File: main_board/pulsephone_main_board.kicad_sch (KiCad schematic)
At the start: 44 parts, among them J1 USB_C_Receptacle_USB2.0_14P, J2 Conn_01x05, J3 Conn_2Rows-35Pins_MountingPin, J4 Conn_2Rows-35Pins_MountingPin, J5 Conn_2Rows-35Pins_MountingPin, U1 XL1509-3.3, U2 PCM5102APWR, U5 TP4056-42-ESOP8

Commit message: add sd card slot. also add rst and onoff buttons
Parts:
- added J7: Micro_SD_Card_Det1, Connector_Card:microSD_HC_Hirose_DM3AT-SF-PEJM5, symbol Connector:Micro_SD_Card_Det1
- added R5, R6: 10 kΩ, Resistor_SMD:R_0805_2012Metric, symbol Device:R
- added SW1, SW2: SW_Push, Button_Switch_SMD:SW_Tactile_SPST_NO_Straight_CK_PTS636Sx25SMTRLFS, symbol Switch:SW_Push
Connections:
- net +3.3V: now also R5.2, R6.2
- net GND: now also J7.6 (VSS), SW1.1, SW2.1
- net SD2_DAT0: now reaches MCM93_MOD1.72 (2)
- net SD2_DAT0: now also J7.7 (DAT0)
- net SD2_DAT1: now reaches MCM93_MOD1.73 (3)
- net SD2_DAT1: now also J7.8 (DAT1)
- net SD2_CD_B: now reaches MCM93_MOD1.74 (4)
- net SD2_CD_B: now also MCM93_MOD1.76 (6), J7.9 (DET)
- net SD2_VDD: now reaches MCM93_MOD1.134 (29)
- net SD2_VDD: now also J7.4 (VDD)
- net RESET: now reaches MCM93_MOD1.14
- net RESET: now also R5.1, SW1.2
- net ONOFF: now reaches MCM93_MOD1.3
- net ONOFF: now also R6.1, SW2.2
- net SD2_RST_B: now reaches MCM93_MOD1.65 (30)
- net SD2_DAT3: now reaches MCM93_MOD1.67 (32)
- net SD2_DAT3: now also J7.2 (DAT3/CD)
- net SD2_DAT2: now reaches MCM93_MOD1.68 (33)
- net SD2_DAT2: now also J7.1 (DAT2)
- net SD2_CMD: now reaches MCM93_MOD1.69 (34)
- net SD2_CMD: now also J7.3 (CMD)
- net SD2_CLK: now reaches MCM93_MOD1.70 (35)
- net SD2_CLK: now also J7.5 (CLK)
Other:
- note added: "Active Low ONOFF"
- note added: "Active Low Reset"
- note added: "MICRO SD"
- moved on the sheet: BT1, C1, C10, C11, C12, C13, C7, C8, C9, D1, D2, H1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

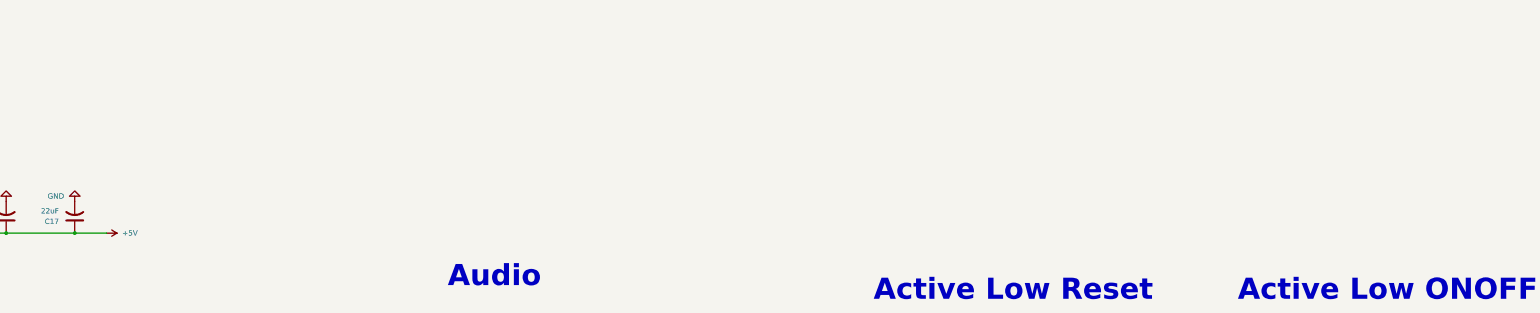
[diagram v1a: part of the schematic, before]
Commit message: more smoothing caps, and making sure board is compliant with CompuLab Standards
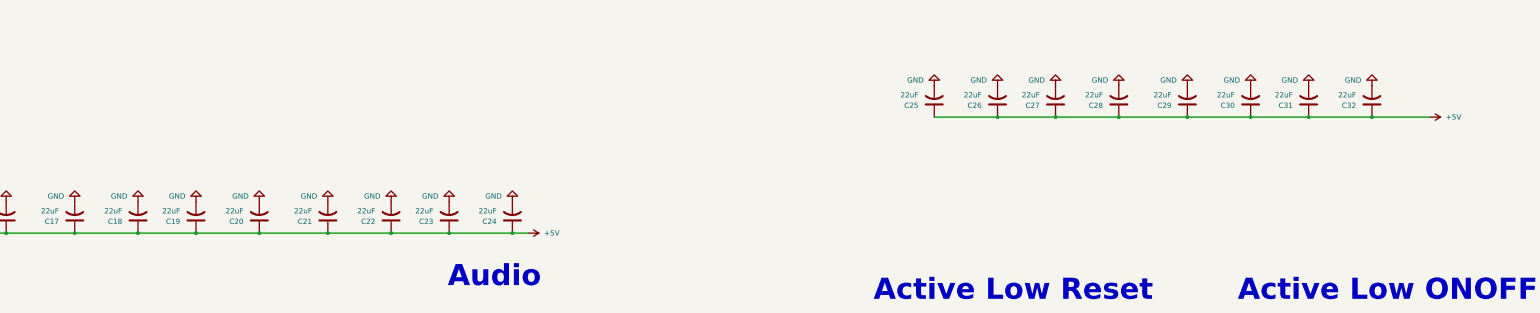
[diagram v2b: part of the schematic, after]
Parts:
- added C18, C19, C20, C21, C22, C23, C24, C25, C26, C27, C28, C29, C30, C31, C32: 22uF, Capacitor_SMD:C_0603_1608Metric, symbol Device:C_US
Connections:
- net +5V: now also C18.1, C19.1, C20.1, C21.1, C22.1, C23.1, C24.1, C25.1, C26.1, C27.1, C28.1, C29.1, C30.1, C31.1, C32.1
- net GND: now also C18.2, C19.2, C20.2, C21.2, C22.2, C23.2, C24.2, C25.2, C26.2, C27.2, C28.2, C29.2, C30.2, C31.2, C32.2

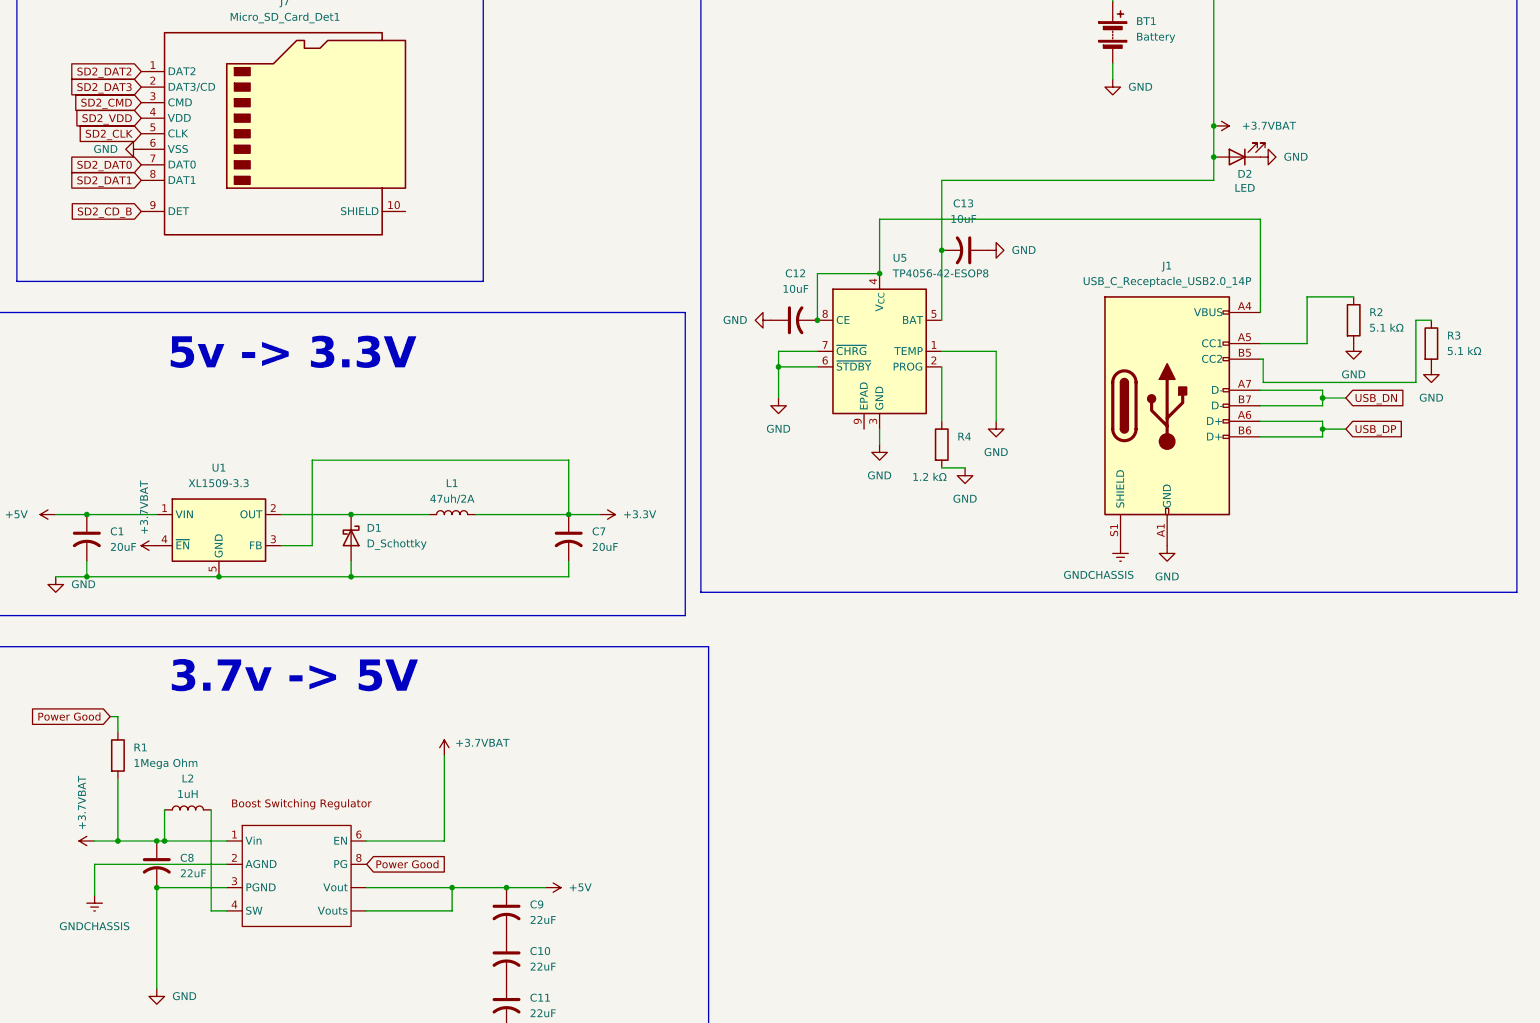
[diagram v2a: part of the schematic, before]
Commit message: fix PCB design errors, and fix power LED circuitry.
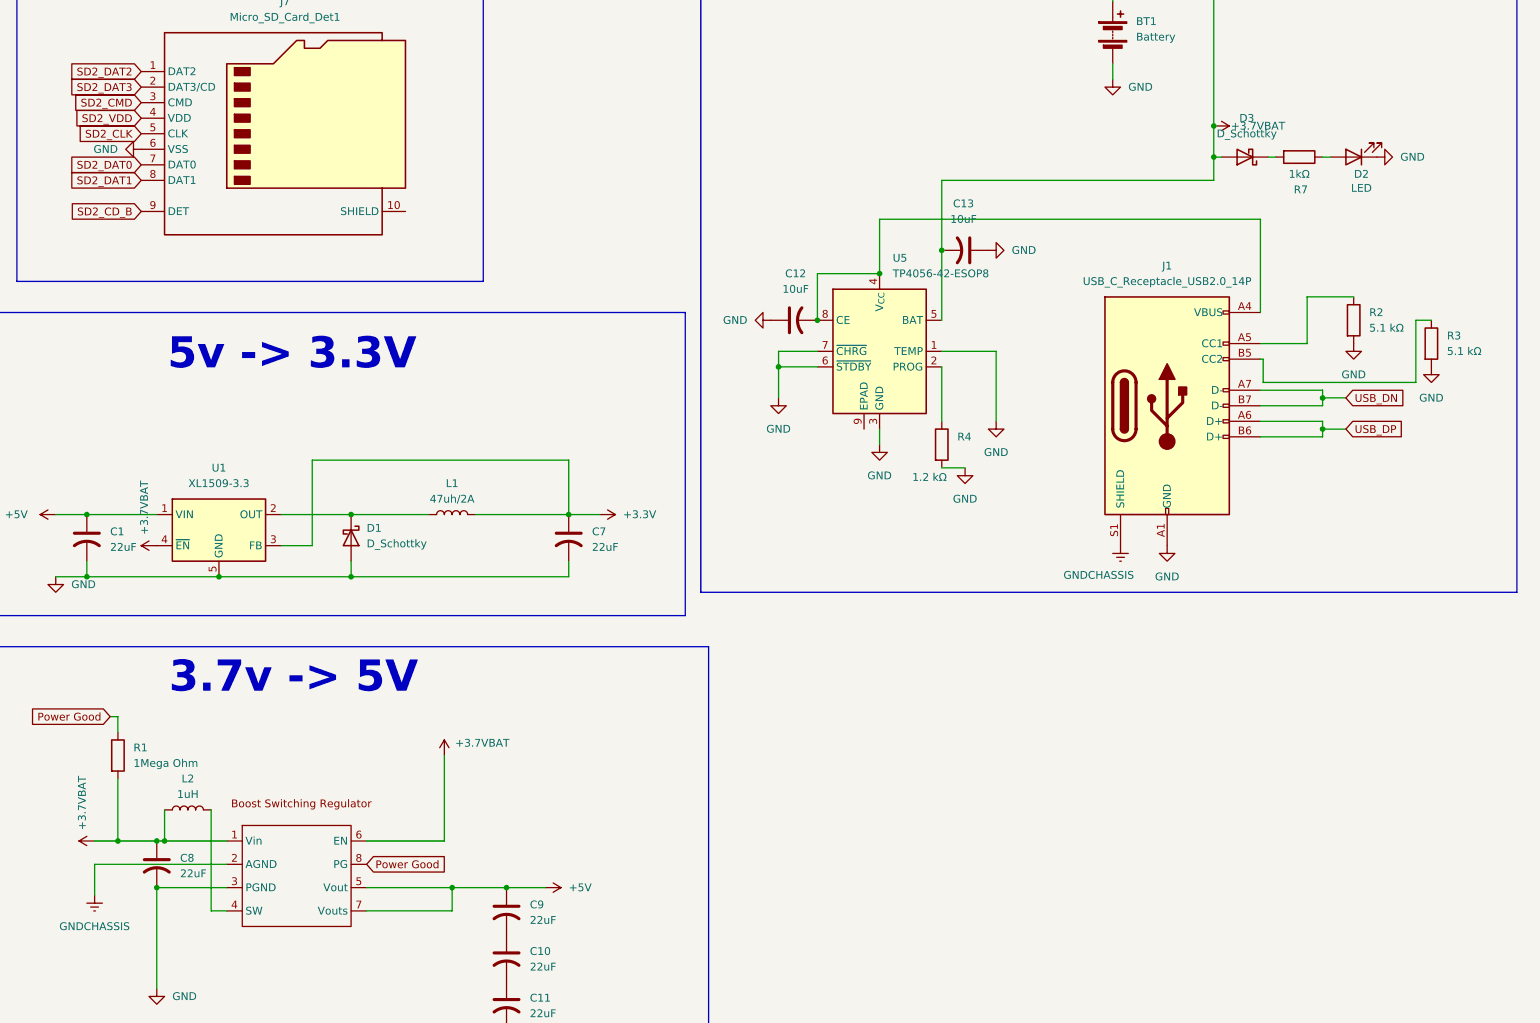
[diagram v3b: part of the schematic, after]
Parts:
- added D3: D_Schottky, Diode_SMD:D_SMA, symbol Device:D_Schottky
- added R7: 1kΩ, Resistor_SMD:R_0805_2012Metric, symbol Device:R
- C1, C7: value 20uF -> 22uF
- D1: footprint Diode_SMD:D_0201_0603Metric -> Diode_SMD:D_SMA
- L1: footprint Inductor_SMD:L_0201_0603Metric -> Inductor_SMD:L_APV_APH0650
- L2: footprint Inductor_SMD:L_0201_0603Metric -> Inductor_SMD_Wurth:L_Wurth_WE-LQSH-4020
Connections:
- net +3.7VBAT: now also D3.2 (A); no longer D2.2 (A)
- net +5V: now also U3.5 (Vout), U3.7 (Vouts); no longer U3. (Vouts)
- new net: D2.2 (A), R7.1
- new net: D3.1 (K), R7.2
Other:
- moved on the sheet: D2
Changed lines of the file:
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@@
 	(wire
 		(pts
+			(xy 725.17 379.73) (xy 723.9 379.73)
+		)
+		(stroke
+			(width 0)
+			(type default)
+		)
+	)
+	(wire
+		(pts
 			(xy 714.1948 416.56) (xy 739.14 416.56)
 		)
@@
 	(wire
 		(pts
+			(xy 716.28 379.73) (xy 715.01 379.73)
+		)
+		(stroke
+			(width 0)
+			(type default)
+		)
+	)
+	(wire
+		(pts
 			(xy 504.19 168.91) (xy 510.54 168.91)
 		)
@@
 	(wire
 		(pts
+			(xy 707.39 379.73) (xy 706.12 379.73)
+		)
+		(stroke
+			(width 0)
+			(type default)
+		)
+	)
+	(wire
+		(pts
 			(xy 538.48 166.37) (xy 538.48 167.64)
 		)
@@
 			)
 		)
-		(pin ""
+		(pin "7"
 		)
 		(pin "2"
@@
 		(pin "6"
 		)
-		(pin ""
+		(pin "5"
 		)
 		(instances
@@
 			)
 		)
-		(property "Value" "20uF"
+		(property "Value" "22uF"
 			(at 604.52 443.4839 0)
 			(effects
@@
 	)
 	(symbol
+		(lib_id "Device:R")
+		(at 720.09 379.73 270)
+		(unit 1)
+		(exclude_from_sim no)
+		(in_bom yes)
+		(on_board yes)
+		(dnp no)
+		(property "Reference" "R7"
+			(at 720.344 385.064 90)
+			(effects
+				(font
+					(size 1.27 1.27)
+				)
+			)
+		)
+		(property "Value" "1kΩ"
+			(at 720.09 382.524 90)
+			(effects
+				(font
+					(size 1.27 1.27)
+				)
+			)
+		)
+		(property "Footprint" "Resistor_SMD:R_0805_2012Metric"
+			(at 720.09 377.952 90)
+			(effects
+				(font
+					(size 1.27 1.27)
+				)
+				(hide yes)
+			)
+		)
+		(property "Datasheet" "~"
+			(at 720.09 379.73 0)
+			(effects
+				(font
+					(size 1.27 1.27)
+				)
+				(hide yes)
+			)
+		)
+		(property "Description" "Resistor"
+			(at 720.09 379.73 0)
+			(effects
+				(font
+					(size 1.27 1.27)
+				)
+				(hide yes)
+			)
+		)
+		(pin "2"
+		)
+		(pin "1"
+		)
+		(instances
+			(project "pulsephone_main_board"
+				(path "/95397744-6eff-4b94-a4c8-db9ebac7d828"
+					(reference "R7")
+					(unit 1)
+				)
+			)
+		)
+	)
+	(symbol
 		(lib_id "Switch:SW_Push")
 		(at 737.87 185.42 0)
@@
 			)
 		)
-		(property "Footprint" "Diode_SMD:D_0201_0603Metric"
+		(property "Footprint" "Diode_SMD:D_SMA"
 			(at 565.15 441.96 0)
 			(effects
@@
 		)
 		(property "Value" "+3.7VBAT"
-			(at 710.692 374.65 90)
+			(at 708.914 374.65 90)
 			(effects
 				(font
@@
 	(symbol
 		(lib_id "Device:LED")
-		(at 709.93 379.73 180)
+		(at 728.98 379.73 180)
 		(unit 1)
 		(exclude_from_sim no)
@@
 		(dnp no)
 		(property "Reference" "D2"
-			(at 711.2 382.524 0)
+			(at 730.25 382.524 0)
 			(effects
 				(font
@@
 		)
 		(property "Value" "LED"
-			(at 711.2 384.81 0)
+			(at 730.25 384.81 0)
 			(effects
 				(font
@@
 		)
 		(property "Footprint" "LED_SMD:LED_0805_2012Metric"
-			(at 709.93 379.73 0)
+			(at 728.98 379.73 0)
 			(effects
 				(font
@@
 		)
 		(property "Datasheet" "~"
-			(at 709.93 379.73 0)
+			(at 728.98 379.73 0)
 			(effects
 				(font
@@
 		)
 		(property "Description" "Light emitting diode"
-			(at 709.93 379.73 0)
+			(at 728.98 379.73 0)
 			(effects
 				(font
@@
 		)
 		(property "Sim.Pins" "1=K 2=A"
-			(at 709.93 379.73 0)
+			(at 728.98 379.73 0)
 			(effects
 				(font
@@
 		(lib_name "GND_1")
 		(lib_id "power:GND")
-		(at 713.74 379.73 90)
+		(at 732.79 379.73 90)
 		(unit 1)
 		(exclude_from_sim no)
@@
 		(fields_autoplaced yes)
 		(property "Reference" "#PWR042"
-			(at 720.09 379.73 0)
+			(at 739.14 379.73 0)
 			(effects
 				(font
@@
 		)
 		(property "Value" "GND"
-			(at 717.55 379.7299 90)
+			(at 736.6 379.7299 90)
 			(effects
 				(font
@@
 		)
 		(property "Footprint" ""
-			(at 713.74 379.73 0)
+			(at 732.79 379.73 0)
 			(effects
 				(font
@@
 		)
 		(property "Datasheet" ""
-			(at 713.74 379.73 0)
+			(at 732.79 379.73 0)
 			(effects
 				(font
@@
 		)
 		(property "Description" "Power symbol creates a global label with name \"GND\" , ground"
-			(at 713.74 379.73 0)
+			(at 732.79 379.73 0)
 			(effects
 				(font
@@
 			)
 		)
-		(property "Footprint" "Inductor_SMD:L_0201_0603Metric"
+		(property "Footprint" "Inductor_SMD_Wurth:L_Wurth_WE-LQSH-4020"
 			(at 538.48 486.41 0)
 			(effects
@@
 			)
 		)
-		(property "Value" "20uF"
+		(property "Value" "22uF"
 			(at 525.78 443.4839 0)
 			(effects
@@
 			)
 		)
-		(property "Footprint" "Inductor_SMD:L_0201_0603Metric"
+		(property "Footprint" "Inductor_SMD:L_APV_APH0650"
 			(at 581.66 438.15 0)
 			(effects
@@
 					(unit 1)
 				)
+			)
+		)
+	)
+	(symbol
+		(lib_id "Device:D_Schottky")
+		(at 711.2 379.73 180)
+		(unit 1)
+		(exclude_from_sim no)
+		(in_bom yes)
+		(on_board yes)
+		(dnp no)
+		(fields_autoplaced yes)
+		(property "Reference" "D3"
+			(at 711.5175 373.38 0)
+			(effects
+				(font
+					(size 1.27 1.27)
+				)
+			)
+		)
+		(property "Value" "D_Schottky"
+			(at 711.5175 375.92 0)
+			(effects
+				(font
+					(size 1.27 1.27)
+				)
+			)
+		)
+		(property "Footprint" "Diode_SMD:D_SMA"
+			(at 711.2 379.73 0)
+			(effects
+				(font
+					(size 1.27 1.27)
+				)
+				(hide yes)
+			)
+		)
+		(property "Datasheet" "~"
+			(at 711.2 379.73 0)
+			(effects
+				(font
+					(size 1.27 1.27)
+				)
+				(hide yes)
+			)
+		)
+		(property "Description" "Schottky diode"
+			(at 711.2 379.73 0)
+			(effects
+				(font
+					(size 1.27 1.27)
+				)
+				(hide yes)
+			)
+		)
+		(pin "1"
+		)
+		(pin "2"
+		)
+		(instances
+			(project "pulsephone_main_board"
+				(path "/95397744-6eff-4b94-a4c8-db9ebac7d828"
+					(reference "D3")
+					(unit 1)
+				)

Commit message: git stuff
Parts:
- L1: footprint Inductor_SMD:L_APV_APH0650 -> Inductor_SMD:L_APV_APH0630
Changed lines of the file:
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@@
 			)
 		)
-		(property "Footprint" "Inductor_SMD:L_APV_APH0650"
+		(property "Footprint" "Inductor_SMD:L_APV_APH0630"
 			(at 581.66 438.15 0)
 			(effects

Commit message: add 3.7v regulator to VBAT for a stable vbat voltage.
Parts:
- removed D2: LED, LED_SMD:LED_0805_2012Metric, symbol Device:LED
- removed D3: D_Schottky, Diode_SMD:D_SMA, symbol Device:D_Schottky
- added C33, C34: 10uF, Capacitor_SMD:C_0603_1608Metric, symbol Device:C_US
- added C35, C36, C37: 22uF, Capacitor_SMD:C_0603_1608Metric, symbol Device:C_US
- added C43: 100nF, Capacitor_SMD:C_0603_1608Metric, symbol Device:C_US
- added CLK-N1, CLK-P1, D0-N1, D0-P1, D1-N1, D1-P1, D2-N1, D2-P1, D3-N1, D3-P1: TestPoint, TestPoint:TestPoint_Pad_1.0x1.0mm, symbol Connector:TestPoint
- added D4: D_Schottky, Diode_SMD:D_SMA, symbol Device:D_Schottky
- added D5: LED, LED_SMD:LED_0805_2012Metric, symbol Device:LED
- added L3: 1.5uH, Inductor_SMD_Wurth:L_Wurth_WE-LQSH-4020, symbol Device:L
- added R10: 1 MΩ, Resistor_SMD:R_0805_2012Metric, symbol Device:R
- added R11: 51 kΩ, Resistor_SMD:R_0805_2012Metric, symbol Device:R
- added R8: 1kΩ, Resistor_SMD:R_0805_2012Metric, symbol Device:R
- added R9: 180 kΩ, Resistor_SMD:R_0805_2012Metric, symbol Device:R
- added U4: TPS63020DSJR/3.7V Reg, TPS63020:IC_TPS63020DSJR, symbol TPS63020DSJR:TPS63020DSJR
- 3.3V1: renamed from TP3; footprint TestPoint:TestPoint_Pad_2.5x2.5mm -> TestPoint:TestPoint_Pad_1.0x1.0mm
- 5V1: renamed from TP2; footprint TestPoint:TestPoint_Pad_2.5x2.5mm -> TestPoint:TestPoint_Pad_1.0x1.0mm
- GND1: renamed from TP1; footprint TestPoint:TestPoint_Pad_2.5x2.5mm -> TestPoint:TestPoint_Pad_1.0x1.0mm
- H1, H2, H3, H4: footprint MountingHole:MountingHole_3.2mm_M3 -> MountingHole:MountingHole_2.2mm_M2_DIN965_Pad
- R7: value 1kΩ -> 1.1 MΩ
- VBAT1: renamed from TP4; footprint TestPoint:TestPoint_Pad_2.5x2.5mm -> TestPoint:TestPoint_Pad_1.0x1.0mm
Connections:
- net +3.7VBAT: now also R7.1, C36.2, D4.2 (A), R10.1, U4.4 (VOUT_4), U4.5 (VOUT_5); no longer BT1.1 (+), C13.2, U5.5 (BAT)
- net DSI_CLK_N: now also CLK-N1.1
- net DSI_CLK_P: now also CLK-P1.1
- net DSI_D0_N: now also D0-N1.1
- net DSI_D0_P: now also D0-P1.1
- net DSI_D1_N: now also D1-N1.1
- net DSI_D1_P: now also D1-P1.1
- net DSI_D2_N: now also D2-N1.1
- net DSI_D2_P: now also D2-P1.1
- net DSI_D3_N: now also D3-N1.1
- net DSI_D3_P: now also D3-P1.1
- net GND: now also C34.1, C37.1, C43.1, D5.1 (K), R9.2, U4.15 (PGND), U4.2 (GND)
- net at R7.2: now also R11.1
- new net: C33.1, C34.2
- new net: BT1.1 (+), C13.2, C33.2, U4.10 (VIN_10), U4.11 (VIN_11), U5.5 (BAT)
- new net: C35.1, C37.2
- new net: C35.2, C36.1
- new net: D4.1 (K), R8.2
- new net: C43.2, U4.1 (VINA), U4.12 (EN), U4.13 (PS/SYNC)
- new net: R11.2, R9.1, U4.3 (FB)
- new net: D5.2 (A), R8.1
- new net L_1: L3.1, U4.8 (L1_8), U4.9 (L1_9)
- new net L_2: L3.2, U4.6 (L2_6), U4.7 (L2_7)
- new net PG2: R10.2, U4.14 (PG)
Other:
- moved on the sheet: BT1, C12, C13, J1, R2, R3, R4, U5
